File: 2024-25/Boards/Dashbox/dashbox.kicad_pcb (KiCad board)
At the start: 2 copper layers, 90 x 75 mm, 15 parts, among them J1 Conn_01x06_Socket, J2 Conn_01x06_Socket, J3 Conn_01x06_Socket, U1 SN65HVD230

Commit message: dashbox pcb
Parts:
- added C4: 1uF/50V, Capacitor_SMD:C_0805_2012Metric_Pad1.18x1.45mm_HandSolder, F.Cu at (135.9, 89.9)
- C1: footprint Capacitor_THT:CP_Radial_Tantal_D7.0mm_P5.00mm -> Capacitor_SMD:C_0805_2012Metric_Pad1.18x1.45mm_HandSolder
- C2, C3: footprint Capacitor_THT:C_Axial_L3.8mm_D2.6mm_P7.50mm_Horizontal -> Capacitor_SMD:C_0805_2012Metric_Pad1.18x1.45mm_HandSolder
- J1, J2, J3: value Conn_01x06_Socket -> 430450600; footprint Connector_Molex:Molex_Micro-Fit_3.0_43045-0612_2x03_P3.00mm_Vertical -> Connector_Molex:Molex_Micro-Fit_3.0_43045-0600_2x03_P3.00mm_Horizontal
- R1, R2, R3, R4, R5: footprint Resistor_THT:R_Axial_DIN0411_L9.9mm_D3.6mm_P12.70mm_Horizontal -> Resistor_THT:R_Axial_DIN0204_L3.6mm_D1.6mm_P5.08mm_Horizontal
- moved J2 51.2 mm to (168.9, 107.6), turned to 180 degrees
- moved R1 27.2 mm to (149.9, 86.4)
- moved C3 25.0 mm to (157.5, 94.0)
- moved R5 23.9 mm to (153.7, 91.4)
- moved R4 23.2 mm to (149.9, 91.4)
- moved R3 21.5 mm to (153.7, 106.7)
- moved R2 20.7 mm to (149.9, 106.7)
- moved C2 19.8 mm to (153.7, 103.1)
- moved Teensy4.1 17.6 mm to (168.9, 72.4), turned to 0 degrees
- moved U1 16.9 mm to (142.2, 59.7), turned to 180 degrees
- moved RE46C2 7.76 mm to (138.4, 86.4), turned to 0 degrees
- moved J1 4.58 mm to (127.5, 64.2)
- moved J3 4.57 mm to (127.5, 105.0)
- moved C1 4.33 mm to (135.9, 104.1), turned to -90 degrees
- moved RE46C1 3.93 mm to (138.4, 100.3), turned to 0 degrees
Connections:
- C1 pad 2: SPK_GND -> GND
- J1 pad 1: CANH -> Net-(J1-Pin_1)
- J1 pad 2: CANL -> Net-(J1-Pin_2)
- J1 pad 3: Net-(J1-Pin_3) -> GND
- J1 pad 4: Net-(J1-Pin_4) -> 5V+
- J1 pad 5: SPK_GND -> CANH
- J1 pad 6: /TNSY_5V+ -> CANL
- J2 pad 1: Speaker1_F -> Speaker1_G
- J2 pad 2: Speaker1_G -> Speaker1_F
- J3 pad 1: SPK_12V+ -> unconnected-(J3-Pin_1-Pad1)
- J3 pad 2: SPK_GND -> GND
- J3 pad 3: Reset -> R2D
- J3 pad 4: /TNSY_5V+ -> 5V+
- J3 pad 5: R2D -> SPK_12V+
- J3 pad 6: /TNSY_5V+ -> 5V+
- RE46C1 pad 5: SPK_GND -> GND
- RE46C2 pad 5: SPK_GND -> GND
- Teensy4.1 pad 7: Net-(J1-Pin_4) -> Net-(J1-Pin_2)
- Teensy4.1 pad 8: Net-(J1-Pin_3) -> Net-(J1-Pin_1)
- Teensy4.1 pad GND1: SPK_GND -> GND
- Teensy4.1 pad GND3: Net-(U1-GND) -> unconnected-(Teensy4.1-GND-PadGND3)
- Teensy4.1 pad VIN: /TNSY_5V+ -> 5V+
- U1 pad 2: Net-(U1-GND) -> unconnected-(U1-GND-Pad2)
- U1 pad 5: Net-(U1-GND) -> unconnected-(U1-Vref-Pad5)
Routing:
- net /TNSY_5V+: track 135.3 -> 0.00 mm
- net SPK_GND: track 131.9 -> 0.00 mm, vias 1 -> 0
- net Net-(J1-Pin_4): track 107.4 -> 0.00 mm
- net SPK_12V+: track 96.0 -> 25.5 mm
- net Net-(J1-Pin_3): track 60.2 -> 0.00 mm
- net R2D: track 91.1 -> 35.3 mm, vias 2 -> 1
- net Net-(RE46C1-HRNEN): track 52.3 -> 3.81 mm, vias 3 -> 0
- net Net-(J1-Pin_2): track 0.00 -> 44.8 mm
- net 5V+: track 0.00 -> 44.2 mm, vias 0 -> 1
- net Net-(J1-Pin_1): track 0.00 -> 41.5 mm
- net Net-(U1-GND): track 39.2 -> 0.00 mm
- net Speaker2_F: track 55.8 -> 22.5 mm, vias 2 -> 0
- net CANH: track 41.5 -> 9.56 mm, vias 2 -> 0
- net CANL: track 41.0 -> 9.54 mm, vias 1 -> 0
- net Net-(Teensy4.1-CTX1): track 38.0 -> 7.27 mm, vias 0 -> 1
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- added copper zone on B.Cu, net GND

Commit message: Dash
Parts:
- added C5: 100nF, Capacitor_SMD:C_0805_2012Metric_Pad1.18x1.45mm_HandSolder, F.Cu at (150.6, 59.8)
- added D1: PESD1CAN, Package_TO_SOT_SMD:SOT-23, F.Cu at (135.1, 59.7)
- added J4: Conn_01x05_Socket, Connector_Wire:SolderWire-0.1sqmm_1x05_P3.6mm_D0.4mm_OD1mm, F.Cu at (166.5, 60.8)
- added R6: 120, Resistor_THT:R_Axial_DIN0204_L3.6mm_D1.6mm_P2.54mm_Vertical, F.Cu at (139.6, 58.5)
- moved Teensy4.1 5.97 mm to (174.9, 72.4)
- moved U1 3.11 mm to (145.3, 59.7)
- moved C3 1.56 mm to (158.8, 94.9), turned to 180 degrees
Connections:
- Teensy4.1 pad 13: unconnected-(Teensy4.1-Pad13) -> Net-(J4-Pin_5)
- Teensy4.1 pad 14: unconnected-(Teensy4.1-TX3-Pad14) -> Net-(J4-Pin_4)
- Teensy4.1 pad 15: unconnected-(Teensy4.1-RX3-Pad15) -> Net-(J4-Pin_3)
- Teensy4.1 pad 16: unconnected-(Teensy4.1-RX4-Pad16) -> Net-(J4-Pin_2)
- Teensy4.1 pad 17: unconnected-(Teensy4.1-TX4-Pad17) -> Net-(J4-Pin_1)
- U1 pad 2: unconnected-(U1-GND-Pad2) -> GND
- U1 pad 8: unconnected-(U1-Rs-Pad8) -> GND
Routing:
- net Net-(RE46C1-HRNEN): track 3.81 -> 19.5 mm
- net 5V+: track 44.2 -> 57.5 mm
- net GND: track 3.26 -> 13.6 mm, vias 2 -> 5
- net 3.3V: track 7.48 -> 0.00 mm
- net Net-(J1-Pin_2): track 44.8 -> 51.9 mm
- net Net-(J1-Pin_1): track 41.5 -> 48.2 mm
- net R2D: track 35.3 -> 41.5 mm, vias 1 -> 2
- net Net-(Teensy4.1-CRX1): track 8.66 -> 13.9 mm
- net Net-(J4-Pin_5): track 0.00 -> 5.00 mm
- net Net-(J4-Pin_1): track 0.00 -> 4.80 mm
- net Net-(J4-Pin_4): track 0.00 -> 4.39 mm
- net Net-(J4-Pin_2): track 0.00 -> 4.36 mm
- net Net-(J4-Pin_3): track 0.00 -> 3.96 mm
- net CANH: track 9.56 -> 13.1 mm
- net CANL: track 9.54 -> 13.0 mm
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- added copper zone on F.Cu, net 3.3V

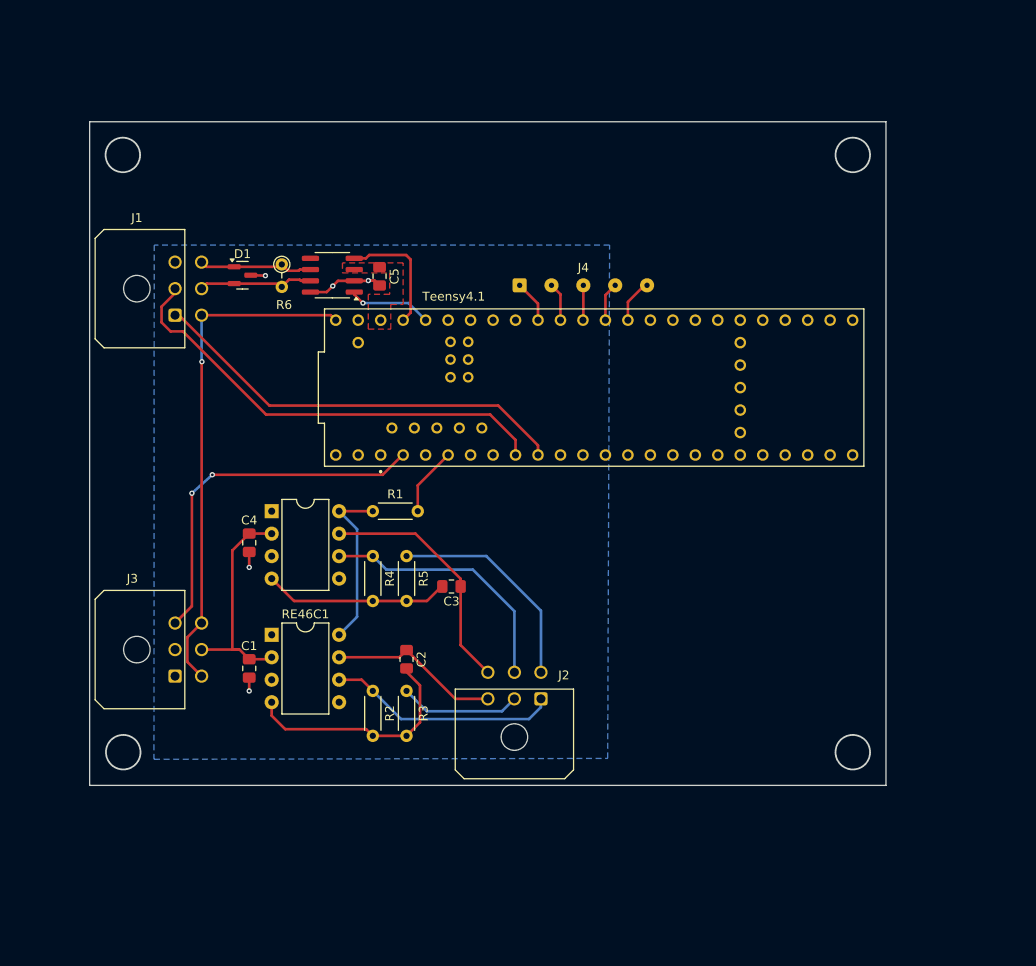
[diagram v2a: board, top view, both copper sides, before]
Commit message: fixed precharge layout
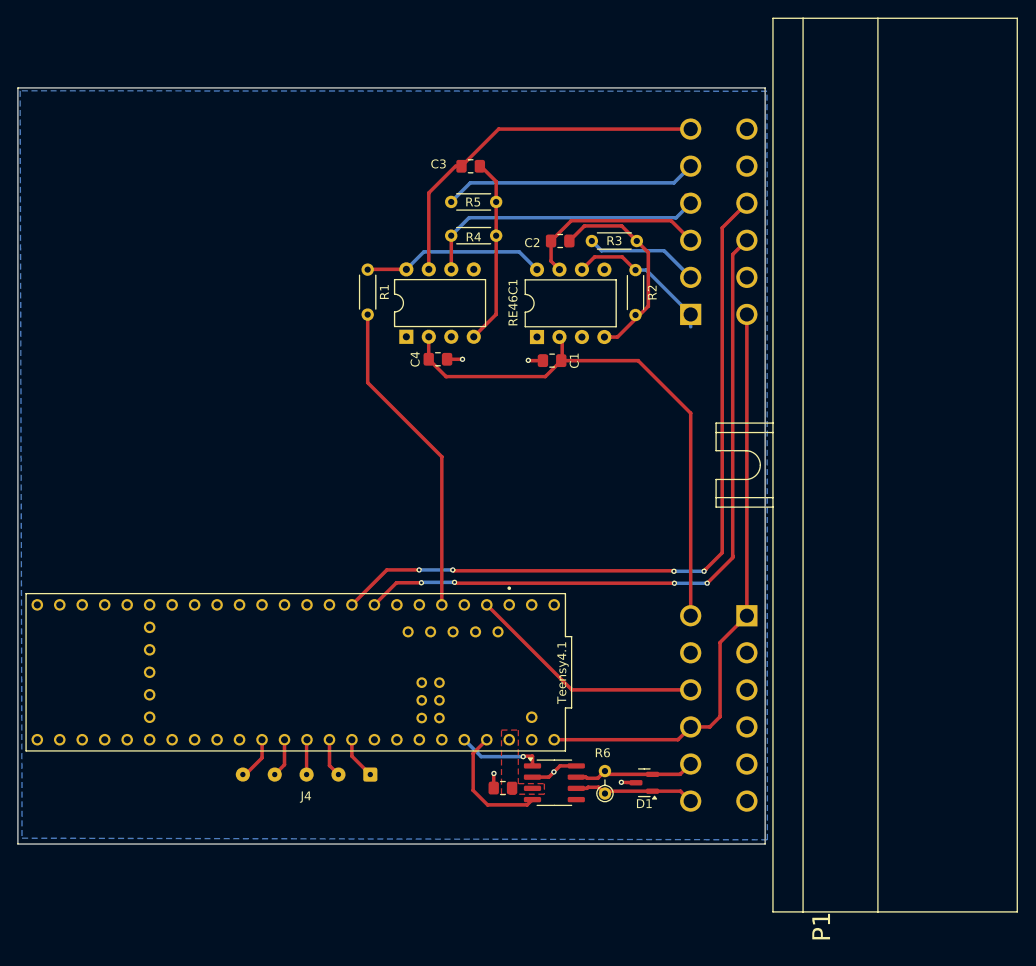
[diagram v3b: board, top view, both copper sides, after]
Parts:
- removed J1, J2, J3: 430450600, Connector_Molex:Molex_Micro-Fit_3.0_43045-0600_2x03_P3.00mm_Horizontal
- added P1: DTM1312PC12PDR008, footprints:TE_DTM1312PC12PDR008, F.Cu at (190.2, 81.2)
- moved D1 73.2 mm to (180.5, 117.1), turned to 180 degrees
- moved R6 70.1 mm to (176.1, 118.3), turned to 90 degrees
- moved U1 62.6 mm to (170.4, 117.1), turned to 0 degrees
- moved C5 59.5 mm to (164.6, 117.7), turned to 180 degrees
- moved J4 57.8 mm to (149.6, 116.1), turned to 180 degrees
- moved R2 56.1 mm to (179.6, 59.1)
- moved R3 55.0 mm to (174.6, 55.8), turned to 0 degrees
- moved C2 50.4 mm to (171.0, 55.8), turned to 0 degrees
- moved C1 48.8 mm to (170.1, 69.3), turned to 180 degrees
- moved C3 47.5 mm to (160.9, 47.4), turned to 0 degrees
- moved Teensy4.1 46.6 mm to (141.2, 104.6), turned to 180 degrees
- moved RE46C1 45.1 mm to (168.4, 66.7), turned to 90 degrees
- moved R5 40.3 mm to (158.7, 51.4), turned to 0 degrees
- moved R4 37.3 mm to (158.7, 55.2), turned to 0 degrees
- moved C4 29.7 mm to (157.2, 69.2), turned to 0 degrees
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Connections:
- Teensy4.1 pad 7: Net-(J1-Pin_2) -> Teensy_RX
- Teensy4.1 pad 8: Net-(J1-Pin_1) -> Teensy_TX
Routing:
- net Teensy_TX: track 0.00 -> 85.5 mm, vias 0 -> 4
- net Teensy_RX: track 0.00 -> 79.6 mm, vias 0 -> 4
- net Net-(J1-Pin_2): track 51.9 -> 0.00 mm
- net Net-(J1-Pin_1): track 48.2 -> 0.00 mm
- net SPK_12V+: track 25.5 -> 62.1 mm
- net Buzz_Enable: track 7.77 -> 36.3 mm
- net R2D: track 41.5 -> 27.0 mm, vias 2 -> 0
- net Speaker2_M: track 27.7 -> 41.2 mm
- net Speaker1_G: track 26.2 -> 16.6 mm
- net 5V+: track 57.5 -> 66.5 mm, vias 1 -> 0
- net Speaker2_F: track 24.7 -> 30.1 mm
- net Speaker2_G: track 29.3 -> 33.7 mm
- net Net-(RE46C1-FEED): track 26.6 -> 23.3 mm
- net Speaker1_M: track 19.4 -> 21.3 mm
- net Net-(RE46C1-HRNEN): track 19.5 -> 20.8 mm
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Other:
- board size 90 x 75 mm -> 84.4 x 85.4 mm

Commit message: Dash added LDO
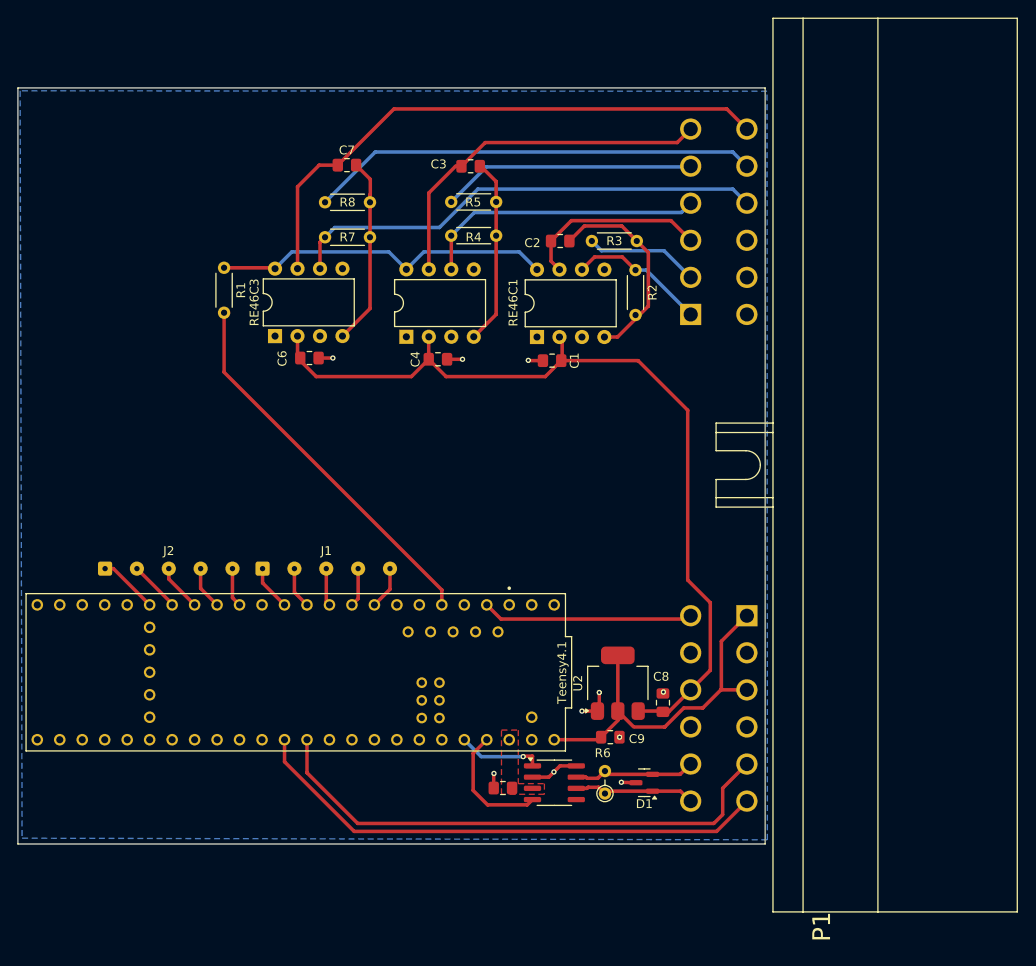
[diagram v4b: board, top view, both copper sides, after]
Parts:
- removed J4: Conn_01x05_Socket, Connector_Wire:SolderWire-0.1sqmm_1x05_P3.6mm_D0.4mm_OD1mm
- added C6: 1uF/50V, Capacitor_SMD:C_0805_2012Metric_Pad1.18x1.45mm_HandSolder, F.Cu at (142.7, 69.0)
- added C7: 1200pF, Capacitor_SMD:C_0805_2012Metric_Pad1.18x1.45mm_HandSolder, F.Cu at (146.9, 47.2)
- added C8: 10uF, Capacitor_SMD:C_0805_2012Metric_Pad1.18x1.45mm_HandSolder, F.Cu at (182.7, 108.0)
- added C9: 10uF, Capacitor_SMD:C_0805_2012Metric_Pad1.18x1.45mm_HandSolder, F.Cu at (176.7, 111.9)
- added J1: Conn_01x05_Socket, Connector_Wire:SolderWire-0.1sqmm_1x05_P3.6mm_D0.4mm_OD1mm, F.Cu at (137.4, 92.8)
- added J2: Conn_01x05_Socket, Connector_Wire:SolderWire-0.1sqmm_1x05_P3.6mm_D0.4mm_OD1mm, F.Cu at (119.6, 92.8)
- added R7: 1.5M, Resistor_THT:R_Axial_DIN0204_L3.6mm_D1.6mm_P5.08mm_Horizontal, F.Cu at (144.5, 55.4)
- added R8: 150k, Resistor_THT:R_Axial_DIN0204_L3.6mm_D1.6mm_P5.08mm_Horizontal, F.Cu at (144.5, 51.5)
- added RE46C3: ~, Package_DIP:DIP-8_W7.62mm, F.Cu at (138.8, 66.6)
- added U2: NCP1117-5.0_SOT223, Package_TO_SOT_SMD:SOT-223-3_TabPin2, F.Cu at (177.6, 105.8)
- moved R1 16.2 mm to (133.1, 58.9)
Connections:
- P1 pad C10: R2D -> SPK_12V+
- P1 pad C12: SPK_12V+ -> R2D
- P1 pad C3: unconnected-(P1-PadC3) -> 5V+
- P1 pad C4: unconnected-(P1-PadC4) -> GND
- P1 pad C5: unconnected-(P1-PadC5) -> Teensy_RX
- P1 pad C6: unconnected-(P1-PadC6) -> Teensy_TX
- P1 pad C9: 5V+ -> unconnected-(P1-PadC9)
- P1 pad D10: Teensy_RX -> unconnected-(P1-PadD10)
- P1 pad D11: GND -> unconnected-(P1-PadD11)
- P1 pad D12: 5V+ -> unconnected-(P1-PadD12)
- P1 pad D7: unconnected-(P1-PadD7) -> Speaker3_M
- P1 pad D8: unconnected-(P1-PadD8) -> Speaker3_F
- P1 pad D9: Teensy_TX -> Speaker3_G
- Teensy4.1 pad 10: unconnected-(Teensy4.1-Pad10) -> Net-(J1-Pin_2)
- Teensy4.1 pad 11: unconnected-(Teensy4.1-Pad11) -> Net-(J1-Pin_1)
- Teensy4.1 pad 13: Net-(J4-Pin_5) -> unconnected-(Teensy4.1-Pad13)
- Teensy4.1 pad 14: Net-(J4-Pin_4) -> Teensy_TX
- Teensy4.1 pad 15: Net-(J4-Pin_3) -> Teensy_RX
- Teensy4.1 pad 16: Net-(J4-Pin_2) -> unconnected-(Teensy4.1-RX4-Pad16)
- Teensy4.1 pad 17: Net-(J4-Pin_1) -> unconnected-(Teensy4.1-TX4-Pad17)
- Teensy4.1 pad 24: unconnected-(Teensy4.1-TX6-Pad24) -> Net-(J2-Pin_4)
- Teensy4.1 pad 25: unconnected-(Teensy4.1-RX6-Pad25) -> Net-(J2-Pin_3)
- Teensy4.1 pad 26: unconnected-(Teensy4.1-Pad26) -> Net-(J2-Pin_2)
- Teensy4.1 pad 27: unconnected-(Teensy4.1-Pad27) -> Net-(J2-Pin_1)
- Teensy4.1 pad 3.3V_1: (no net) -> Net-(J2-Pin_5)
- Teensy4.1 pad 7: Teensy_RX -> Net-(J1-Pin_5)
- Teensy4.1 pad 8: Teensy_TX -> Net-(J1-Pin_4)
- Teensy4.1 pad 9: unconnected-(Teensy4.1-Pad9) -> Net-(J1-Pin_3)
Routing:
- net Speaker3_M: track 0.00 -> 64.6 mm
- net Speaker3_G: track 0.00 -> 54.4 mm
- net Speaker3_F: track 0.00 -> 50.7 mm
- net SPK_12V+: track 62.1 -> 97.4 mm
- net Teensy_TX: track 85.5 -> 59.4 mm, vias 4 -> 0
- net 5V+: track 66.5 -> 41.9 mm
- net Net-(RE46C3-FEED): track 0.00 -> 21.8 mm
- net Teensy_RX: track 79.6 -> 60.3 mm, vias 4 -> 0
- net Net-(RE46C1-HRNEN): track 20.8 -> 38.7 mm
- net Buzz_Enable: track 36.3 -> 43.2 mm
- net Net-(J2-Pin_1): track 0.00 -> 6.74 mm
- net Net-(J2-Pin_2): track 0.00 -> 5.75 mm
- net GND: track 12.4 -> 17.8 mm, vias 5 -> 10
- net Net-(J2-Pin_3): track 0.00 -> 5.31 mm
- net Net-(J1-Pin_1): track 0.00 -> 5.12 mm
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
